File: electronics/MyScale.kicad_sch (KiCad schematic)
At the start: 19 parts, among them J6 12402012E212A, J7 Conn_01x03, SW1 SW_Push, SW2 SW_Push, U2 ESP32-C6-WROOM-1-N8

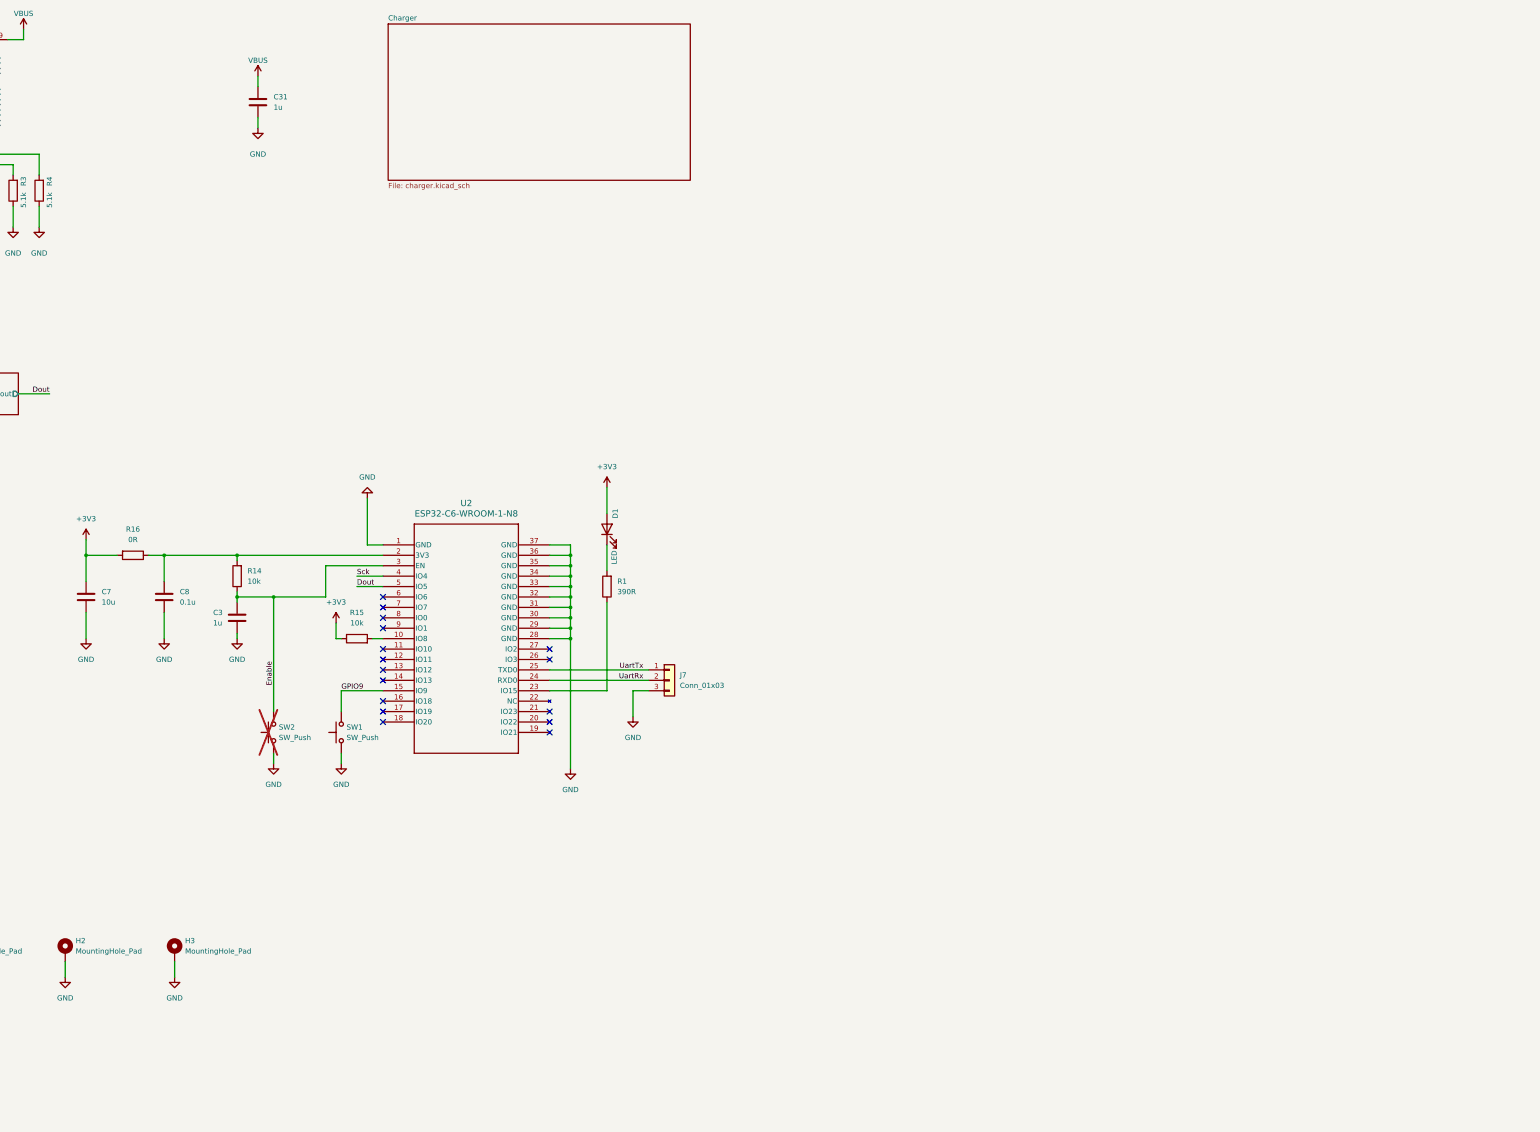
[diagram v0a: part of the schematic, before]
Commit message: electronics: start with A7670 module
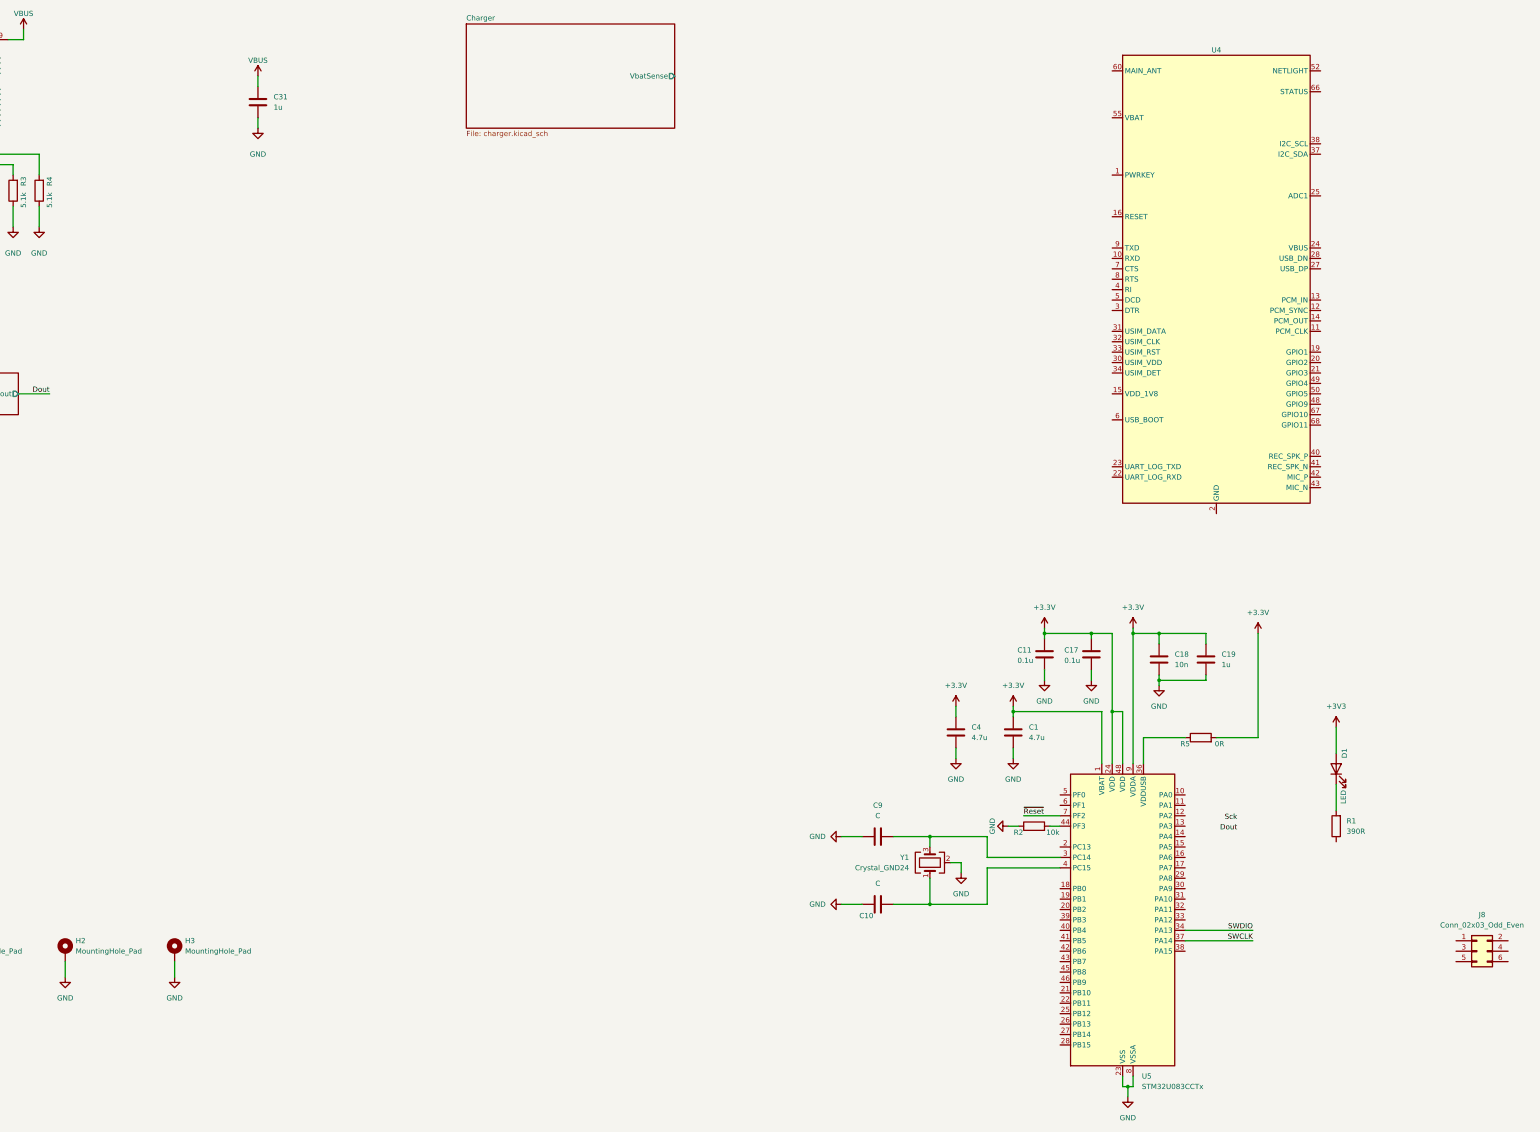
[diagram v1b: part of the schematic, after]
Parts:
- removed C3: 1u, Capacitor_SMD:C_0603_1608Metric, symbol Device:C
- removed C7: 10u, Capacitor_SMD:C_0603_1608Metric, symbol Device:C
- removed C8: 0.1u, Capacitor_SMD:C_0603_1608Metric, symbol Device:C
- removed J7: Conn_01x03, Connector_PinHeader_2.54mm:PinHeader_1x03_P2.54mm_Vertical, symbol Connector_Generic:Conn_01x03
- removed R14, R15: 10k, Resistor_SMD:R_0603_1608Metric, symbol Device:R
- removed R16: 0R, Resistor_SMD:R_0603_1608Metric, symbol Device:R
- removed SW1, SW2: SW_Push, Button_Switch_SMD:SW_SPST_TL3305A, symbol Switch:SW_Push
- removed U2: ESP32-C6-WROOM-1-N8, MyScale:MOD28_ESP32-C6-WROOM-1_EXP, symbol MyScale:ESP32-C6-WROOM-1-N8
- added C1, C4: 4.7u, symbol Device:C
- added C10, C9: C, symbol Device:C
- added C11, C17: 0.1u, symbol Device:C
- added C18: 10n, symbol Device:C
- added C19: 1u, symbol Device:C
- added J8: Conn_02x03_Odd_Even, symbol Connector_Generic:Conn_02x03_Odd_Even
- added R2: 10k, symbol Device:R
- added R5: 0R, symbol Device:R
- added U4: (no value), MyScale:A7670, symbol MyScale:A7670
- added U5: STM32U083CCTx, Package_QFP:LQFP-48_7x7mm_P0.5mm, symbol MCU_ST_STM32U0:STM32U083CCTx
- added Y1: Crystal_GND24, symbol Device:Crystal_GND24
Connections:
- net GND: now also C1.2, C10.1, C11.2, C17.2, C18.2, C19.2, C4.2, C9.1, R2.1, U4.17 (GND), U4.18 (GND), U4.2 (GND), U4.29 (GND), U4.39 (GND), U4.45 (GND), U4.46 (GND), U4.54 (GND), U4.58 (GND), U4.59 (GND), U4.61 (GND), U4.62 (GND), U4.63 (GND), U4.64 (GND), U4.65 (GND), U4.69 (GND), U4.70 (GND), U4.71 (GND), U4.72 (GND), U4.73 (GND), U4.74 (GND), U4.75 (GND), U4.76 (GND), U4.77 (GND), U4.78 (GND), U4.79 (GND), U4.80 (GND), U4.81 (GND), U4.82 (GND), U4.83 (GND), U4.84 (GND), U4.85 (GND), U4.86 (GND), U4.87 (GND), U4.88 (GND), U5.23 (VSS), U5.35 (VSS), U5.47 (VSS), U5.8 (VSSA), Y1.2 (G), Y1.4 (G)
- new net: C9.2, U5.3 (PC14), Y1.3
- new net: C10.2, U5.4 (PC15), Y1.1
- new net: R2.2, U5.44 (PF3)
- new net: U4.26 (NC), U4.35 (NC), U4.36 (NC), U4.44 (NC), U4.47 (NC), U4.51 (NC), U4.53 (NC)
- new net: R5.1, U5.36 (VDDUSB)
- new net +3.3V: C1.1, C11.1, C17.1, C18.1, C19.1, C4.1, R5.2, U5.1 (VBAT), U5.24 (VDD), U5.48 (VDD), U5.9 (VDDA)
- new net SWCLK: U5.37 (PA14)
- new net SWDIO: U5.34 (PA13)
- new net VBAT: U4.55 (VBAT), U4.56 (VBAT), U4.57 (VBAT)
- new net ~{Reset}: U5.7 (PF2)
- no-connect marks 22 -> 6
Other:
- sheet Charger ports: added VbatSense; removed none
- moved on the sheet: D1, R1

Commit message: schematics
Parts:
- removed U4: (no value), MyScale:A7670, symbol MyScale:A7670
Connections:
- net +3V3 is gone; now on net +1V8: D1.2 (A)
- net Led: now reaches R1.1
- net +3.3V renamed +1V8
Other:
- added sheet Radio (radio.kicad_sch)
- sheet Load Cell Interface ports: added Enable; removed none

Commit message: electronics: replace charger
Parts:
- removed J8: Conn_02x03_Odd_Even, symbol Connector_Generic:Conn_02x03_Odd_Even
- removed U5: STM32U083CCTx, Package_QFP:LQFP-48_7x7mm_P0.5mm, symbol MCU_ST_STM32U0:STM32U083CCTx
- removed Y1: Crystal_GND24, symbol Device:Crystal_GND24
- added J10: Conn_02x03_Odd_Even, solar-tag:Tag-Connect_TC2030-IDC-NL_2x03_P1.27mm_Vertical, symbol Connector_Generic:Conn_02x03_Odd_Even
- added U5: STM32U083CCUx, Package_DFN_QFN:QFN-48-1EP_7x7mm_P0.5mm_EP5.6x5.6mm, symbol MCU_ST_STM32U0:STM32U083CCUx
- added Y1: Crystal, Crystal:Crystal_SMD_2012-2Pin_2.0x1.2mm, symbol Device:Crystal
- C1, C11, C17, C18, C19, C4: footprint (none) -> Capacitor_SMD:C_0603_1608Metric
- C10, C9: value C -> 6.8p; footprint (none) -> Capacitor_SMD:C_0603_1608Metric
- R2, R5: footprint (none) -> Resistor_SMD:R_0603_1608Metric
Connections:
- net +1V8: now also U5.1 (VBAT), U5.24 (VDD), U5.48 (VDD), U5.9 (VDDA)
- net GND: now also J10.1 (Pin_1), U5.23 (VSS), U5.35 (VSS), U5.47 (VSS), U5.49 (VSS), U5.8 (VSSA)
- net SWCLK: now also U5.37 (PA14)
- net SWDIO: now also J10.5 (Pin_5), U5.34 (PA13)
- net ~{Reset}: now also U5.7 (PF2)
- net at C9.2: now also U5.3 (PC14), Y1.2
- net at C10.2: now also U5.4 (PC15), Y1.1
- net at R2.2: now also U5.44 (PF3)
- net at R5.1: now also U5.36 (VDDUSB)
- net USBD+: now reaches J6.A6 (D+)
- net USBD+: now also J6.B6 (D+)
- net USBD-: now reaches J6.A7 (D-)
- net USBD-: now also J6.B7 (D-)
- new net SWDCLK: J10.6 (Pin_6)
- new net UartRx: J10.3 (Pin_3)
- new net UartTx: J10.4 (Pin_4)
- new net VCC: J10.2 (Pin_2)
- new net VbatSense: U5.10 (PA0)
- no-connect marks 6 -> 2
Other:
- sheet Radio ports: added PwrKeySet; removed none

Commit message: electronics: initial placement
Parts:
- J10: footprint solar-tag:Tag-Connect_TC2030-IDC-NL_2x03_P1.27mm_Vertical -> Connector:Tag-Connect_TC2030-IDC-NL_2x03_P1.27mm_Vertical
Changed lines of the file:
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@@
 			)
 		)
-		(property "Footprint" "solar-tag:Tag-Connect_TC2030-IDC-NL_2x03_P1.27mm_Vertical"
+		(property "Footprint" "Connector:Tag-Connect_TC2030-IDC-NL_2x03_P1.27mm_Vertical"
 			(at 416.56 201.93 0)
 			(hide yes)

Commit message: electronics: start routing
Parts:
- added C43: 0.1u, Capacitor_SMD:C_0603_1608Metric, symbol Device:C
- added R7: 10k, Resistor_SMD:R_0603_1608Metric, symbol Device:R
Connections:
- net +1V8: now also R7.2
- net GND: now also C43.2
- net ~{Reset}: now also C43.1, R7.1

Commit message: electronics: sync
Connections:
- net SWDCLK is gone; now on net SWCLK: J10.6 (Pin_6)
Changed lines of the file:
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@@
 		)
 	)
-	(label "SWDCLK"
+	(label "SWCLK"
 		(at 430.53 204.47 0)
 		(effects

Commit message: electronics: replace A7670 footprint
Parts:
- added J8: Conn_01x02_MountingPin, MyScale:JST_S2B-PH-SM4-TB(LF)(SN), symbol Connector_Generic_MountingPin:Conn_01x02_MountingPin
- added R27, R28: 27R, Resistor_SMD:R_0603_1608Metric, symbol Device:R
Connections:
- net VCC is gone; now on net +1V8: J10.2 (Pin_2)
- net CellsEnable: now also U5.16 (PA6)
- net Dout: now also U5.25 (PB12)
- net GND: now also J8.2 (Pin_2), J8.MP (MountPin)
- net Led: now also U5.13 (PA3)
- net RadioEnable: now also U5.40 (PB4)
- net RadioPwrKey: now also U5.12 (PA2)
- net RadioUartRx: now also U5.17 (PA7)
- net RadioUartTx: now also U5.15 (PA5)
- net Sck: now also U5.26 (PB13)
- net USBD+: now also R28.1; no longer J6.A6 (D+), J6.B6 (D+)
- net USBD-: now also R27.1; no longer J6.A7 (D-), J6.B7 (D-)
- net UartRx: now also U5.31 (PA10)
- net UartTx: now also U5.30 (PA9)
- net VBUS: now also J8.1 (Pin_1)
- new net USBCD+: J6.A6 (D+), J6.B6 (D+), R28.2
- new net USBCD-: J6.A7 (D-), J6.B7 (D-), R27.2
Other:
- moved on the sheet: C1, C10, C11, C17, C18, C19, C4, C43, C9, H1, H2, H3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

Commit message: electronics: final touches
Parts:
- added TP3, TP4: TestPoint, TestPoint:TestPoint_Pad_D1.0mm, symbol Connector:TestPoint
- R27, R28: now not fitted; now left out of the parts list
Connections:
- net Dout: now also U5.26 (PB13); no longer U5.25 (PB12)
- net RadioUartRx: now also TP4.1
- net RadioUartTx: now also TP3.1
- net Sck: now also U5.25 (PB12); no longer U5.26 (PB13)
- net BatSenseEnable: now reaches U5.46 (PB9)
- no-connect marks 2 -> 23
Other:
- sheet Charger ports: added BatSenseEnable; removed none
